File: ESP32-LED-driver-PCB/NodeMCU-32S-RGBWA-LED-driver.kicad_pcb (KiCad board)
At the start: 2 copper layers, 50 x 50 mm, 25 parts, among them J1 PJ-037AH, J2 TBP02R1-381-05BE, Q1 AO6404, Q2 AO6404, Q3 AO6404, Q4 AO6404, U1 NodeMCU-32S, U2 NCP1117-3.3_SOT223

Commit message: Project description
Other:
- board text added: "5V to 12V. 5A max"
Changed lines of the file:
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@@
     (effects (font (size 1.5 1.5) (thickness 0.3)))
+  )
+  (gr_text "5V to 12V. 5A max" (at 147.8 71.83 90) (layer "F.SilkS")
+    (effects (font (size 0.8 0.8) (thickness 0.2)))
   )
   (gr_text "G" (at 123.75 73.75) (layer "F.SilkS")

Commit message: Updated silkscreen
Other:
- board text added: "For driving addressable LEDs: Remove 0R resistors from R1-R4 Place 0R resistors on R5-R7 Bridge JP1-JP3"
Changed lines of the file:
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@@
   (gr_line (start 128.75 81.95) (end 126.75 81.95) (layer "F.SilkS") (width 0.15))
   (gr_rect (start 109.75 63.05) (end 159.75 113.05) (layer "Edge.Cuts") (width 0.2) (fill none))
+  (gr_text "For driving addressable LEDs:\nRemove 0R resistors from R1-R4\nPlace 0R resistors on R5-R7\nBridge JP1-JP3" (at 158.92 91.94) (layer "B.SilkS")
+    (effects (font (size 1 1) (thickness 0.15)) (justify left mirror))
+  )
   (gr_text "/Dat" (at 121.45 74.75) (layer "F.SilkS")
     (effects (font (size 0.8 0.8) (thickness 0.1)))

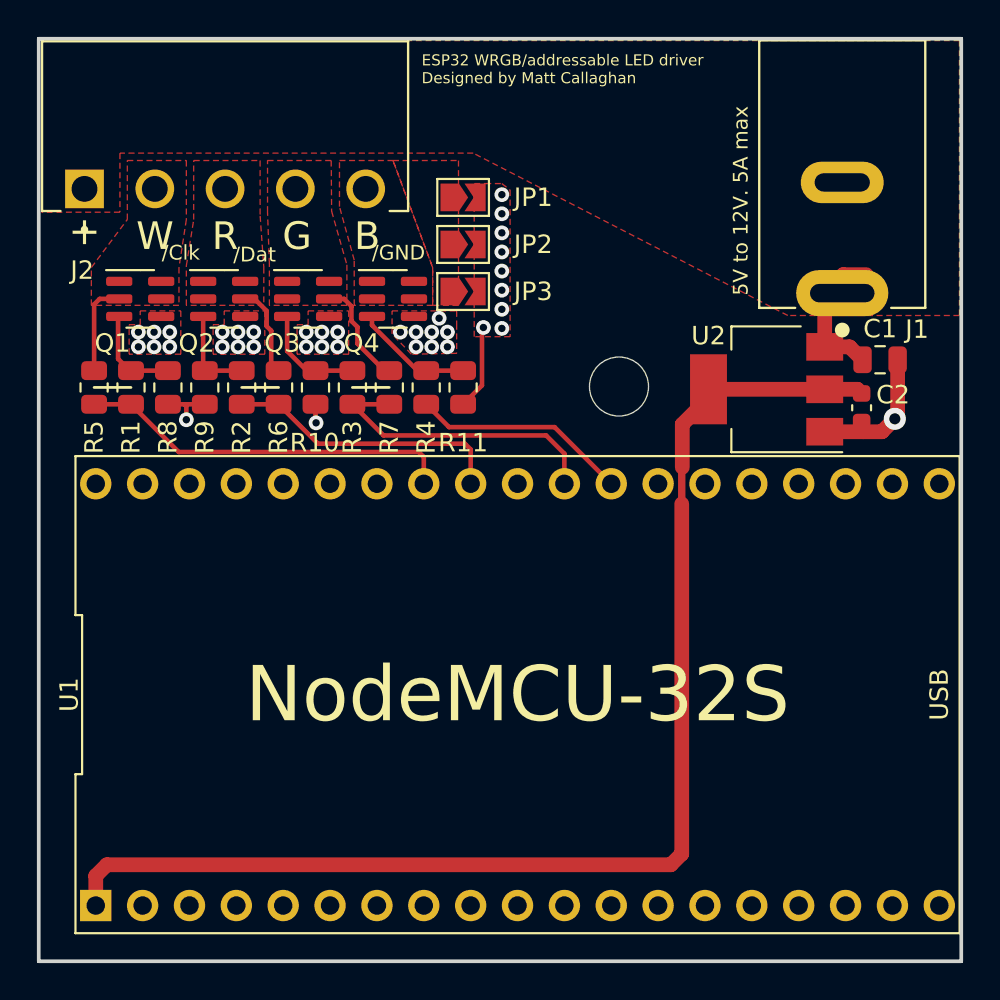
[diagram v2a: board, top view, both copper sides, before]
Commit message: Updated to 6 pin connector
Moved to 6 pin connector to get more addressable outputs with a dedicated ground pin.
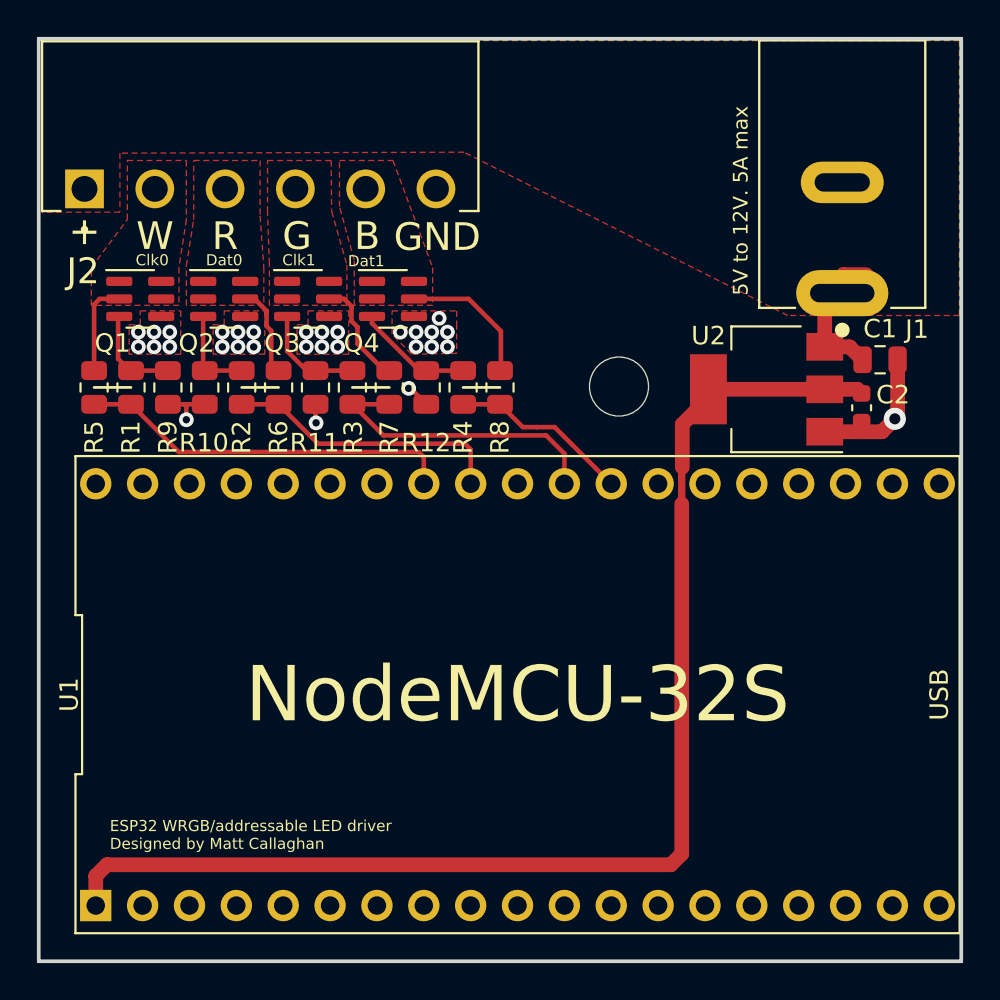
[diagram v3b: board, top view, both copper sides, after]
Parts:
- removed JP1, JP2, JP3: SolderJumper_2_Open, Jumper:SolderJumper-2_P1.3mm_Open_TrianglePad1.0x1.5mm
- added R8: 0805 DNF, Resistor_SMD:R_0805_2012Metric, F.Cu at (134.8, 82.0)
- J1: value PJ-037AH -> PJ-037A
- J2: footprint Matts_Library:CUI_TBP02R1-381-05BE -> Matts_Library:CUI_TBP02R1-381-06BE
- moved R12 2.00 mm to (130.8, 82.0)
- moved R4 2.00 mm to (132.8, 82.0)
- renumbered R9 to R10, R10 to R11, R11 to R12, R8 to R9
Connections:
- net /Blue/GND renamed /Blue/Dat1
- net /Green renamed /Green/Clk1
- net /Red/Dat renamed /Red/Dat0
- net /White/Clk renamed /White/Clk0
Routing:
- net /Blue/Dat1: track 0.00 -> 7.60 mm
- net GND: track 16.4 -> 13.1 mm, vias 38 -> 30
- net Net-(R4-Pad1): track 11.4 -> 9.43 mm
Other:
- board text added: "Clk0"
- board text added: "Clk1"
- board text added: "Dat0"
- board text added: "Dat1"
- board text added: "For driving addressable LEDs: Remove 0R resistors from R1-R4 Place 0R resistors on R5-R8"
- board text added: "GND"
- board text removed: "/Clk"
- board text removed: "/Dat"
- board text removed: "/GND"
- board text removed: "For driving addressable LEDs: Remove 0R resistors from R1-R4 Place 0R resistors on R5-R7 Bridge JP1-JP3"

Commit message: Added prototyping area
Added prototyping area to allow for extra sensors.
Updated some silkscreen
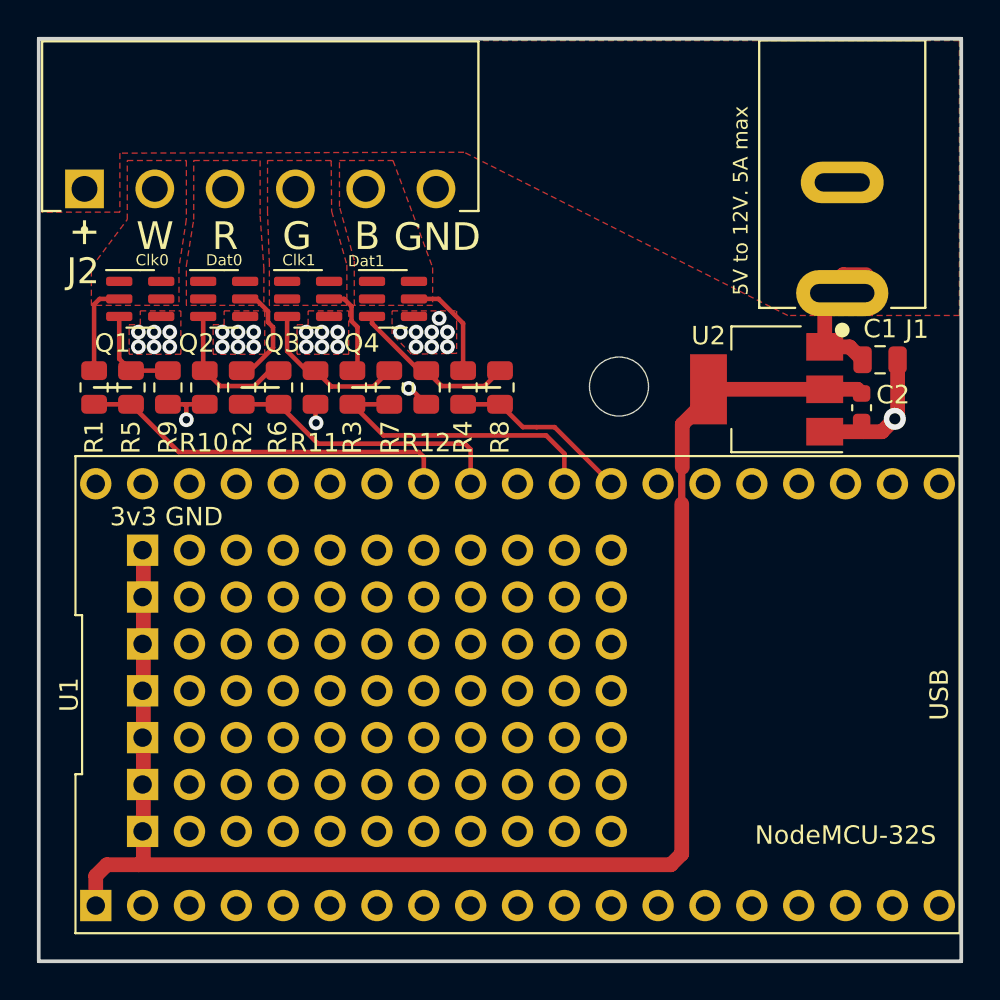
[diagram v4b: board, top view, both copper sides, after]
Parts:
- added J3: Conn_01x11, Matts_Library:PinHeader_1x11_P2.54mm_Vertical, F.Cu at (115.4, 106.0)
- added J4: Conn_01x11, Matts_Library:PinHeader_1x11_P2.54mm_Vertical, F.Cu at (115.4, 103.5)
- added J5: Conn_01x11, Matts_Library:PinHeader_1x11_P2.54mm_Vertical, F.Cu at (115.4, 100.9)
- added J6: Conn_01x11, Matts_Library:PinHeader_1x11_P2.54mm_Vertical, F.Cu at (115.4, 98.4)
- added J7: Conn_01x11, Matts_Library:PinHeader_1x11_P2.54mm_Vertical, F.Cu at (115.4, 95.8)
- added J8: Conn_01x11, Matts_Library:PinHeader_1x11_P2.54mm_Vertical, F.Cu at (115.4, 93.3)
- added J9: Conn_01x11, Matts_Library:PinHeader_1x11_P2.54mm_Vertical, F.Cu at (115.4, 90.8)
- moved R2 2.00 mm to (120.8, 82.0)
- moved R3 2.00 mm to (126.8, 82.0)
- moved R4 2.00 mm to (132.8, 82.0)
- moved R6 2.00 mm to (122.8, 82.0)
- moved R7 2.00 mm to (128.8, 82.0)
- moved R8 2.00 mm to (134.8, 82.0)
- renumbered R5 to R1, R6 to R2, R7 to R3, R8 to R4, R1 to R5, R2 to R6, R3 to R7, R4 to R8
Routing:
- net +3V3: track 69.9 -> 87.1 mm
- net Net-(Q3-Pad2): track 5.85 -> 8.83 mm
- net Net-(Q4-Pad2): track 6.37 -> 9.14 mm
- net Net-(Q2-Pad2): track 4.97 -> 7.67 mm
- net /Blue/Dat1: track 7.60 -> 5.77 mm
- net /Red/Dat0: track 4.94 -> 5.82 mm
- net /Green/Clk1: track 5.87 -> 5.11 mm
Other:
- board text added: "3v3 GND"
- board text added: "GND 3v3"
